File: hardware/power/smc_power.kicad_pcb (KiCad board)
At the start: 4 copper layers, 101 parts, among them IC1 LM393DR2GH, J1 Screw_Terminal_01x02, J2 48V Input, J3 48V Output, J4 24V Brake Output, J5 Logic Output, Q1 P40B10SL, U1 TPS54360DDA, U2 AP2112K-3.3, U3 TPS54360DDA, U4 TPS16630PWPR, U5 MCP1416, U6 TL431B_C54830630, U7 L78L12_SOT89

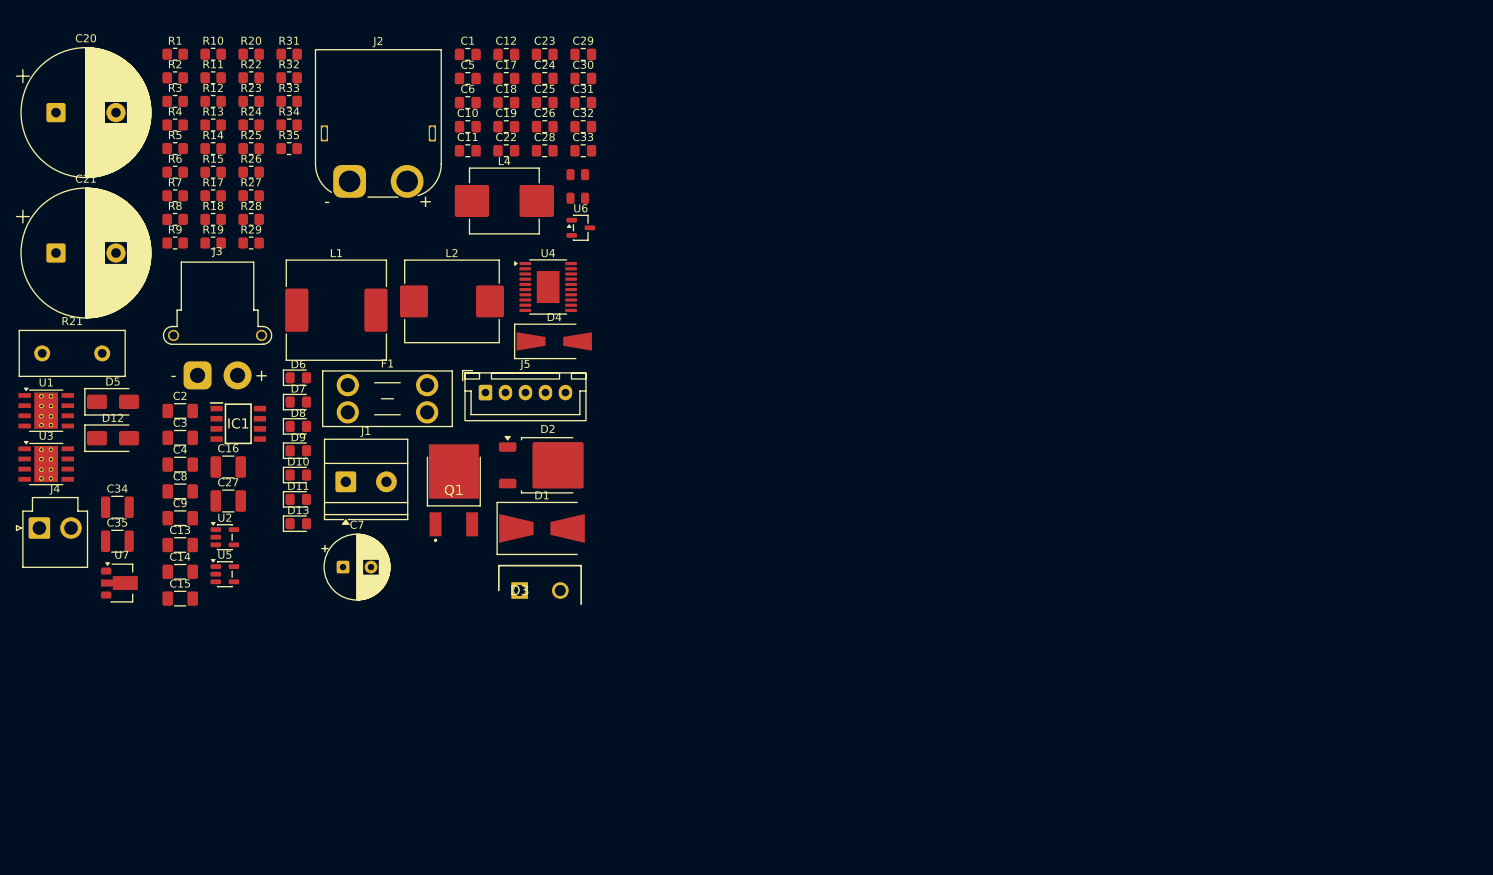
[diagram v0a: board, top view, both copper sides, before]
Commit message: hw(power): board outline, mounting holes, zones, floorplan and chopper/buck/LDO layout, refs #39 #40 #41 #42 #43
Co-Authored-By: Claude Opus 5.5 <noreply@anthropic.com>
Claude-Session: https://claude.ai/code/session_01SoMHYQYx4yCFML8vht6Kpa
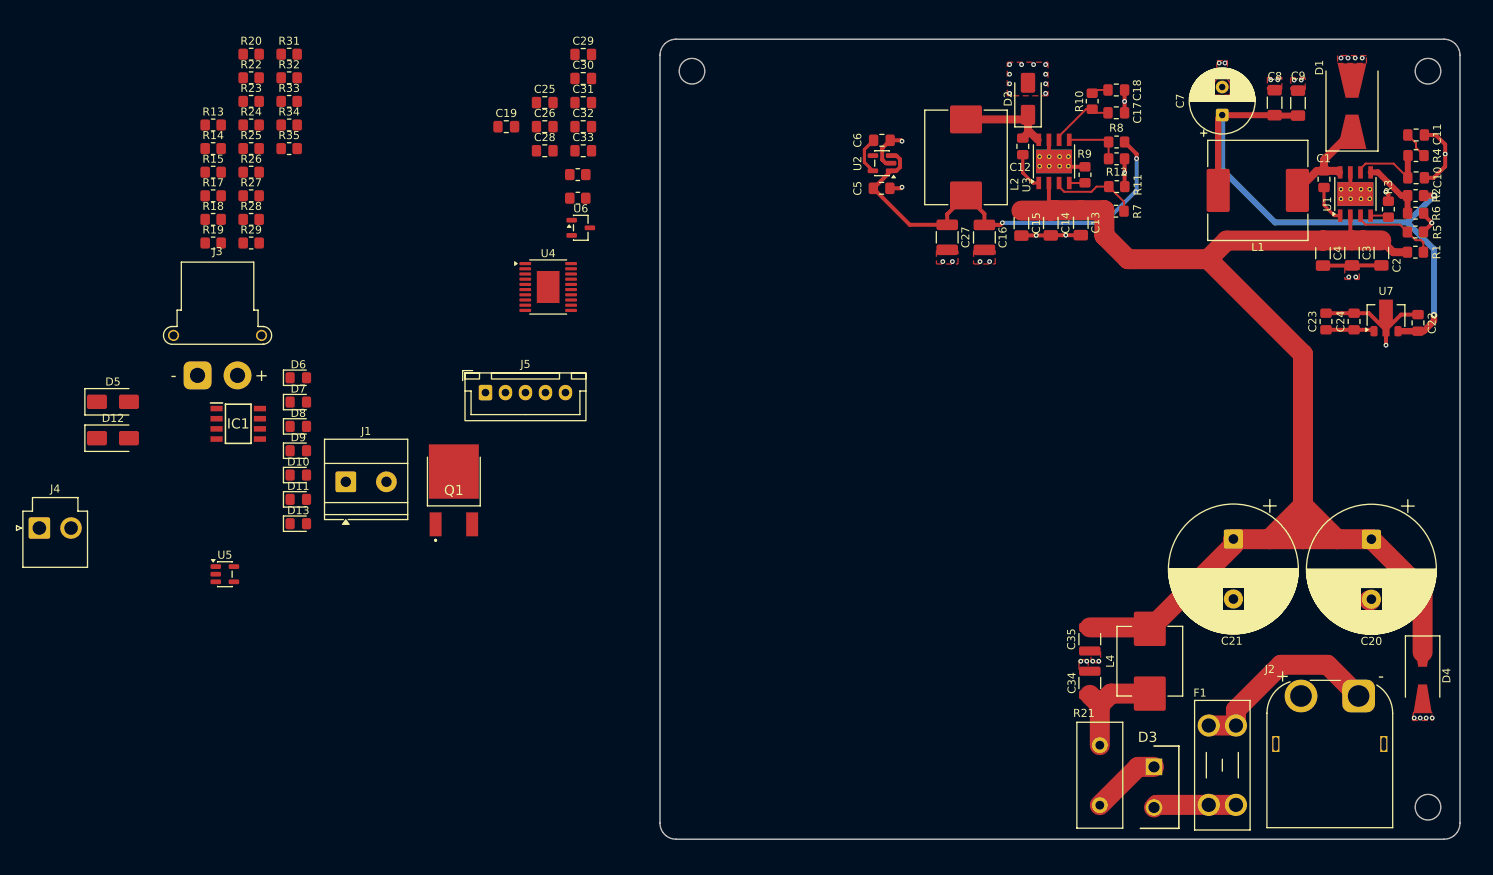
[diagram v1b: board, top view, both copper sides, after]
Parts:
- added H1: MountingHole_M3, MountingHole:MountingHole_3.2mm_M3, F.Cu at (104.0, 24.0)
- added H2: MountingHole_M3, MountingHole:MountingHole_3.2mm_M3, F.Cu at (196.0, 24.0)
- added H3: MountingHole_M3, MountingHole:MountingHole_3.2mm_M3, F.Cu at (196.0, 116.0)
- D2: value 100V 5A -> SS510; footprint Package_TO_SOT_SMD:TO-252-2 -> Diode_SMD:D_SMA
- moved C20 172.9 mm to (188.9, 82.5), turned to -90 degrees
- moved U1 165.9 mm to (186.9, 39.4), turned to 90 degrees
- moved U7 161.5 mm to (190.8, 54.5), turned to 90 degrees
- moved R1 157.0 mm to (194.4, 46.6)
- moved R2 155.8 mm to (194.4, 39.5), turned to 180 degrees
- moved R5 155.4 mm to (194.4, 44.1)
- moved R4 155.2 mm to (194.5, 34.5)
- moved R6 155.1 mm to (194.4, 41.8)
- moved R3 152.3 mm to (191.1, 41.2), turned to 90 degrees
- moved C21 151.5 mm to (171.7, 82.5), turned to -90 degrees
- moved C2 151.4 mm to (190.2, 46.7), turned to -90 degrees
- moved C9 149.0 mm to (179.8, 28.0), turned to 90 degrees
- moved C3 148.3 mm to (186.5, 46.7), turned to -90 degrees
- moved C4 145.3 mm to (182.9, 46.7), turned to -90 degrees
- moved C8 145.2 mm to (176.8, 27.9), turned to 90 degrees
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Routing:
- net +VM: track 0.00 -> 174.1 mm
- net +24V: track 0.00 -> 76.6 mm, vias 0 -> 2
- net GND: track 0.00 -> 66.6 mm, vias 0 -> 44
- net +5V: track 0.00 -> 54.7 mm, vias 0 -> 2
- net +48V: track 0.00 -> 24.6 mm
- net /SW_5V: track 0.00 -> 15.8 mm
- net /VIN_EMI: track 0.00 -> 13.6 mm
- net /SW_24V: track 0.00 -> 13.4 mm
- net Net-(U3-EN): track 0.00 -> 11.3 mm
- net Net-(U1-EN): track 0.00 -> 10.9 mm
- net /VIN_FUSED: track 0.00 -> 10.4 mm
- net Net-(U1-COMP): track 0.00 -> 10.2 mm
- net /VIN_PROT: track 0.00 -> 8.76 mm
- net Net-(U3-COMP): track 0.00 -> 8.15 mm
- net /FB_24V: track 0.00 -> 8.02 mm
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- added copper zone on F.Cu, net GND
- added copper zone on In1.Cu, net GND
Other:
- board outline added: 100 x 100 mm

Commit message: hw(power): complete layout (all blocks placed and routed), refs #39 #40 #41 #42 #43 #68
Co-Authored-By: Claude Opus 5.5 <noreply@anthropic.com>
Claude-Session: https://claude.ai/code/session_01SoMHYQYx4yCFML8vht6Kpa
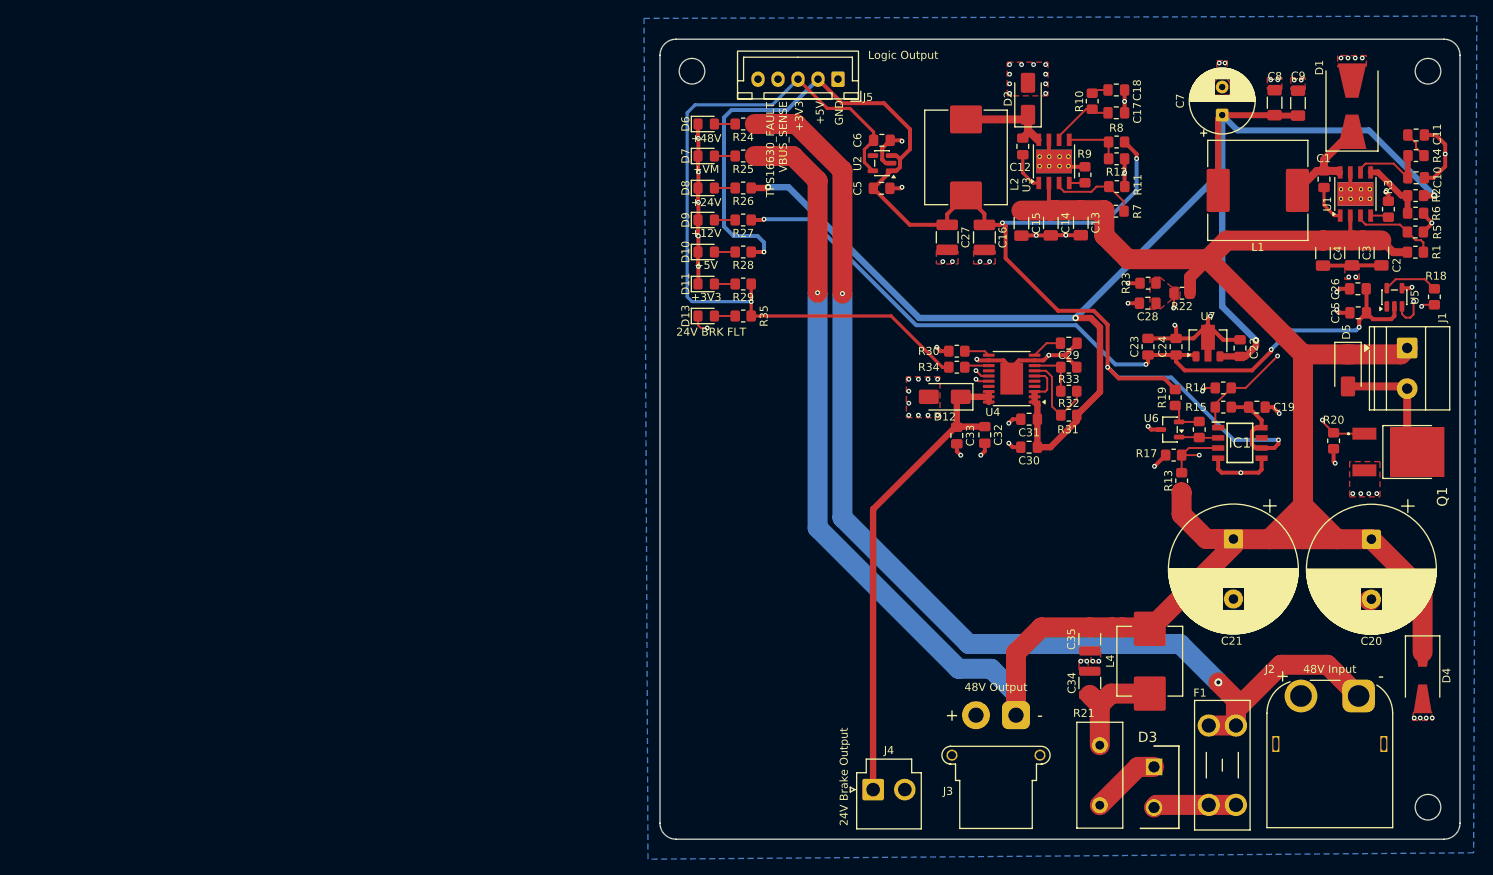
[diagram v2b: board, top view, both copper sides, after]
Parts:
- moved D5 154.4 mm to (186.0, 61.4), turned to -90 degrees
- moved R18 153.0 mm to (196.8, 52.2), turned to -90 degrees
- moved U5 150.2 mm to (191.8, 52.3), turned to 90 degrees
- moved R20 143.7 mm to (184.2, 70.2), turned to -90 degrees
- moved J1 133.7 mm to (193.4, 58.6), turned to -90 degrees
- moved R14 129.8 mm to (170.4, 63.6)
- moved R15 129.6 mm to (170.4, 66.0), turned to 180 degrees
- moved R13 129.0 mm to (165.2, 75.2), turned to 90 degrees
- moved IC1 125.2 mm to (172.5, 70.5)
- moved R17 124.4 mm to (164.2, 72.0), turned to 180 degrees
- moved R19 121.8 mm to (164.4, 64.8), turned to 90 degrees
- moved R22 119.4 mm to (165.2, 51.8), turned to 180 degrees
- moved Q1 118.1 mm to (192.2, 71.6), turned to -90 degrees
- moved R23 114.4 mm to (161.0, 50.5), turned to 180 degrees
- moved J3 110.8 mm to (144.5, 104.5), turned to 180 degrees
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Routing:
- net +VM: track 174.1 -> 311.5 mm, vias 0 -> 1
- net +5V: track 54.7 -> 183.4 mm, vias 2 -> 5
- net +48V: track 24.6 -> 143.2 mm, vias 0 -> 2
- net +24V: track 76.6 -> 194.5 mm, vias 2 -> 4
- net +12V: track 6.07 -> 101.2 mm, vias 0 -> 4
- net +3V3: track 4.73 -> 96.1 mm, vias 0 -> 1
- net GND: track 66.6 -> 143.1 mm, vias 44 -> 81
- net /VBUS_SENSE: track 0.00 -> 67.7 mm, vias 0 -> 1
- net /+24V_BRK: track 0.00 -> 61.9 mm
- net /TPS16630_FLT#: track 0.00 -> 49.6 mm, vias 0 -> 1
- net /TPS16630_PGOOD: track 0.00 -> 40.4 mm, vias 0 -> 2
- net Net-(IC1-OUTPUT_A): track 0.00 -> 37.9 mm, vias 0 -> 2
- net Net-(Q1-G): track 0.00 -> 32.0 mm, vias 0 -> 2
- net Net-(IC1-INPUT_A_2): track 0.00 -> 19.3 mm, vias 0 -> 2
- net /CHOP_DRAIN: track 0.00 -> 16.0 mm
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- added copper zone on F.Cu, net /VBUS_SENSE
- added copper zone on B.Cu, net GND
- added copper zone on In2.Cu, net GND
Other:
- board text added: "+3V3"
- board text added: "+5V"
- board text added: "GND"
- board text added: "TPS16630_FAULT"
- board text added: "VBUS_SENSE"

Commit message: hw(power): J4 +/- silkscreen, refs #39
Co-Authored-By: Claude Opus 5.5 <noreply@anthropic.com>
Claude-Session: https://claude.ai/code/session_01SoMHYQYx4yCFML8vht6Kpa
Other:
- board text added: "+"
- board text added: "-"
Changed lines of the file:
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@@
 		(layer "Margin")
 	)
+	(gr_text "+"
+		(at 126.6 108.4 0)
+		(layer "F.SilkS")
+		(effects
+			(font
+				(size 1 1)
+				(thickness 0.15)
+			)
+		)
+	)
+	(gr_text "-"
+		(at 130.4 108.4 0)
+		(layer "F.SilkS")
+		(effects
+			(font
+				(size 1 1)
+				(thickness 0.15)
+			)
+		)
+	)
 	(gr_text "TPS16630_FAULT"
 		(at 113.8 33.8 90)
@@
 		)
 		(min_thickness 0.25)
-		(fill yes
+		(fill
 			(thermal_gap 0.5)
 			(thermal_bridge_width 0.5)
@@
 		)
 		(min_thickness 0.25)
-		(fill yes
+		(fill
 			(thermal_gap 0.5)
 			(thermal_bridge_width 0.5)
@@
 		)
 		(min_thickness 0.25)
-		(fill yes
+		(fill
 			(thermal_gap 0.5)
 			(thermal_bridge_width 0.5)
@@
 		)
 		(min_thickness 0.25)
-		(fill yes
+		(fill
 			(thermal_gap 0.5)
 			(thermal_bridge_width 0.5)
@@
 		)
 		(min_thickness 0.25)
-		(fill yes
+		(fill
 			(thermal_gap 0.5)
 			(thermal_bridge_width 0.5)
@@
 		)
 		(min_thickness 0.25)
-		(fill yes
+		(fill
 			(thermal_gap 0.5)
 			(thermal_bridge_width 0.5)
@@
 		)
 		(min_thickness 0.25)
-		(fill yes
+		(fill
 			(thermal_gap 0.5)
 			(thermal_bridge_width 0.5)
@@
 		)
 		(min_thickness 0.25)
-		(fill yes
+		(fill
 			(thermal_gap 0.5)
 			(thermal_bridge_width 0.5)
@@
 		)
 		(min_thickness 0.25)
-		(fill yes
+		(fill
 			(thermal_gap 0.5)
 			(thermal_bridge_width 0.5)
@@
 		)
 		(min_thickness 0.25)
-		(fill yes
+		(fill
 			(thermal_gap 0.5)
 			(thermal_bridge_width 0.5)
@@
 		)
 		(min_thickness 0.25)
-		(fill yes
+		(fill
 			(thermal_gap 0.5)
 			(thermal_bridge_width 0.5)
@@
 		)
 		(min_thickness 0.25)
-		(fill yes
+		(fill
 			(thermal_gap 0.5)
 			(thermal_bridge_width 0.5)
@@
 		)
 		(min_thickness 0.25)
-		(fill yes
+		(fill
 			(thermal_gap 0.5)
 			(thermal_bridge_width 0.5)
@@
 		)
 		(min_thickness 0.25)
-		(fill yes
+		(fill
 			(thermal_gap 0.5)
 			(thermal_bridge_width 0.5)
@@
 		)
 		(min_thickness 0.25)
-		(fill yes
+		(fill
 			(thermal_gap 0.5)
 			(thermal_bridge_width 0.5)
